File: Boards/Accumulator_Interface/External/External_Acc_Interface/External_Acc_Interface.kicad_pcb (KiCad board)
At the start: 2 copper layers, 107.2 x 62.8 mm, 5 parts, among them J1 Ampseal_35_VT, J2 SS-126-G-2, J3 BBS-126-G-A, U1 RJ45_VT, U2 RJ45_VT

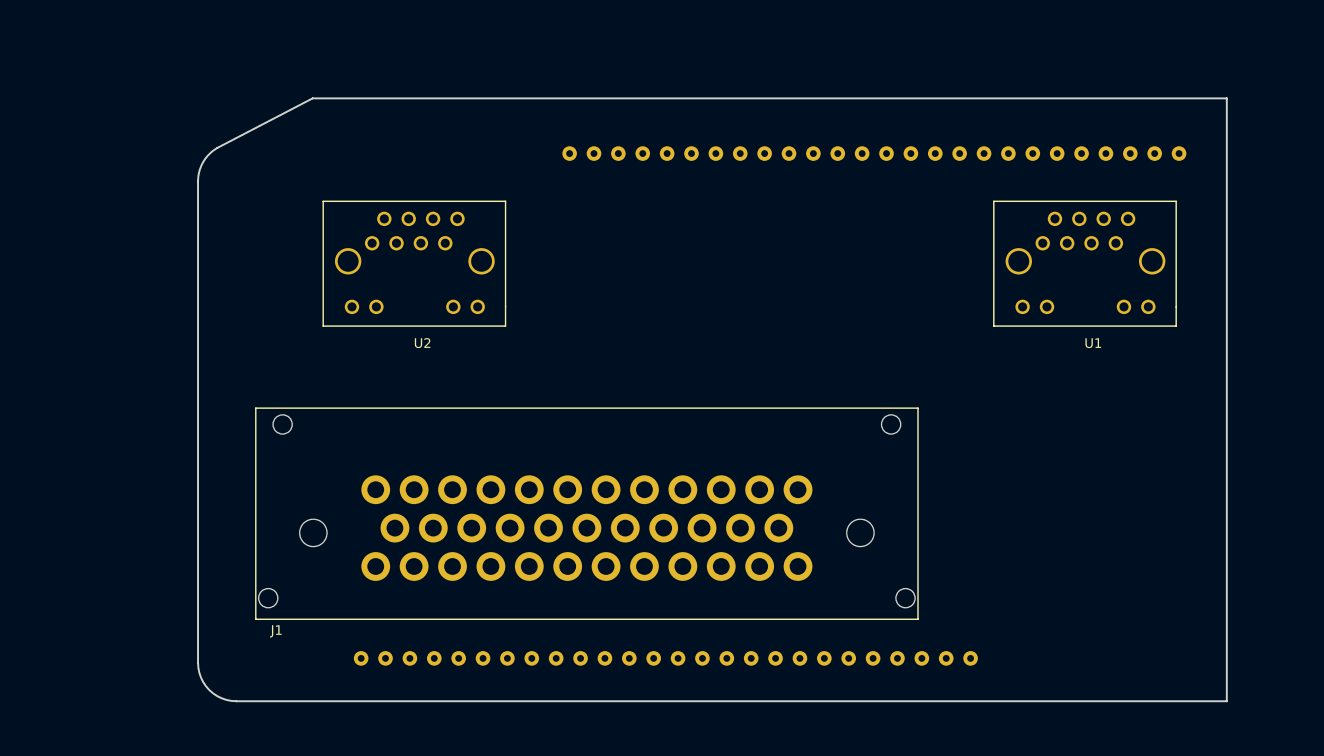
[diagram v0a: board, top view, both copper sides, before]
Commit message: started internal acc interface
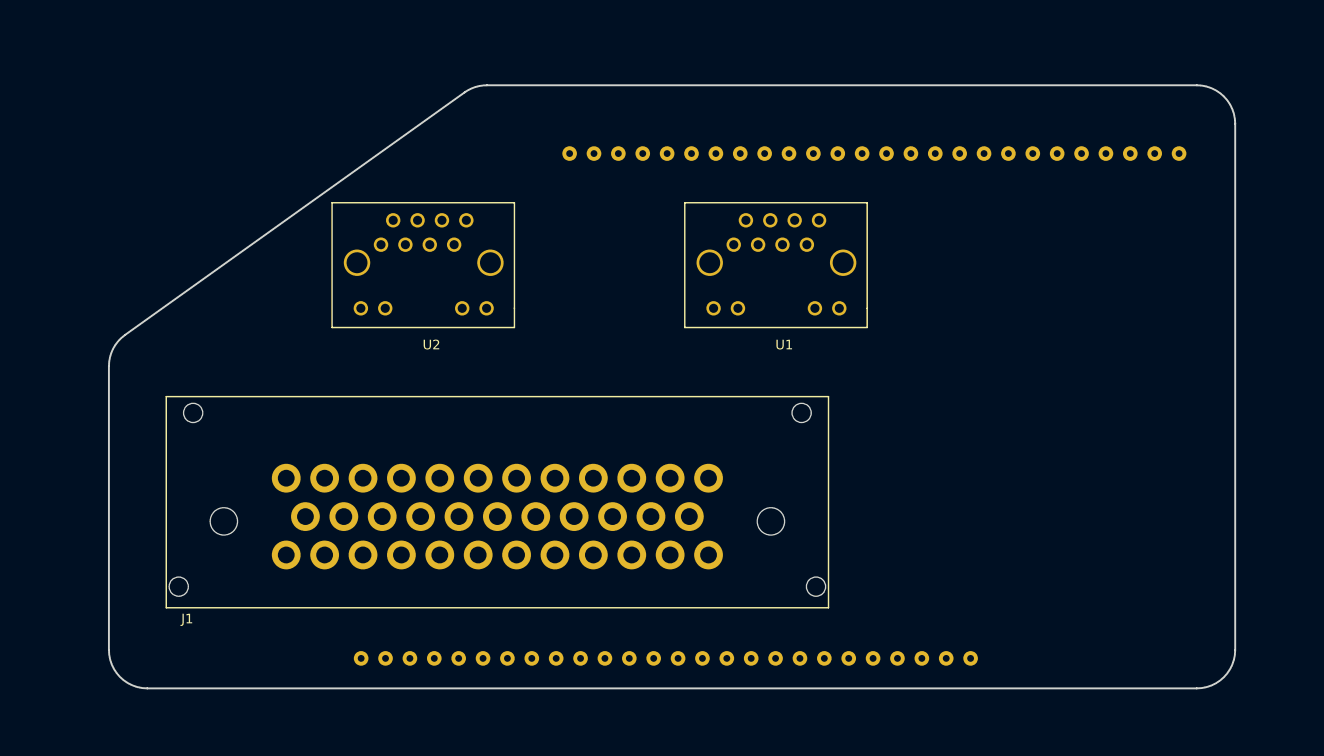
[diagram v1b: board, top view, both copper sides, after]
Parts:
- moved U1 32.2 mm to (53.5, 66.2)
- moved J1 9.40 mm to (2.50, 88.4)
- moved U2 0.94 mm to (16.8, 66.2)
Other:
- board size 107.2 x 62.8 mm -> 117.4 x 62.8 mm

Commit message: first pass of acc interface and rev1.1 of periph layout
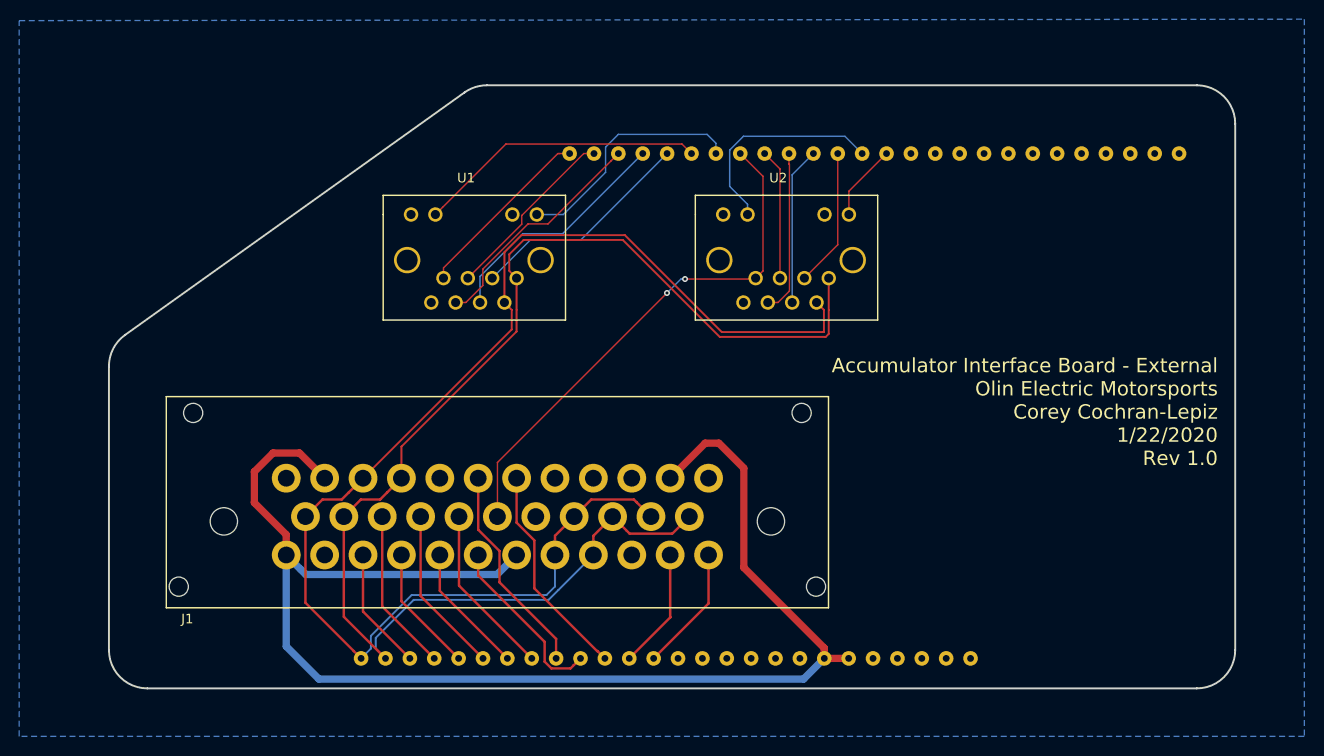
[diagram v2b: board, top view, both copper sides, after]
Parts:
- moved J2 56.9 mm to (16.8, 102.7)
- moved J3 56.9 mm to (38.5, 50.0)
- moved U2 51.8 mm to (67.6, 56.4), turned to 180 degrees
- moved U1 20.9 mm to (35.1, 56.4), turned to 180 degrees
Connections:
- J1 pad 1: /GND -> /CAN-GND
- J1 pad 10: /GND -> /CAN-GND
- J1 pad 12: /GND -> /CAN-GND
- J1 pad 13: /CAN-H -> /CAN_P
- J1 pad 14: /CAN-L -> /CAN_N
- J1 pad 18: /5V-AIR -> /5V_AIRC
- J1 pad 19: /GND -> /CAN-GND
- J1 pad 20: /CAN-H -> /CAN_P
- J1 pad 21: /CAN-L -> /CAN_N
- J1 pad 22: /CAN-H -> /CAN_P
- J1 pad 23: /CAN-L -> /CAN_N
- J1 pad 25: /GND -> /CAN-GND
- J1 pad 3: /CAN-H -> /CAN_P
- J1 pad 31: /CAN-H -> /CAN_P
- J1 pad 32: /CAN-L -> /CAN_N
- J1 pad 4: /CAN-L -> /CAN_N
- J1 pad 8: /GND -> /CAN-GND
- J1 pad 9: /GND -> /CAN-GND
- J2 pad 1: /GND -> /CAN_P
- J2 pad 10: /TSAL-Green-Neg -> /ChargeEnable2
- J2 pad 11: /TSAL-Red-Pos -> /TSMS->FinalShutdown
- J2 pad 12: /TSAL-Red-Neg -> /BSDP-Current-Sense
- J2 pad 13: /GND -> /HVD->HVD-Connector
- J2 pad 14: /HVD->HVD-Connector -> /CAN-GND
- J2 pad 15: /IMD->TSMS -> /CAN-GND
- J2 pad 16: /TSMS->FinalShutdown -> /CAN-GND
- J2 pad 17: /GND -> /CAN-GND
- J2 pad 18: /GND -> /CAN-GND
- J2 pad 19: /GND -> /CAN-GND
- J2 pad 2: /12V -> /CAN_N
- J2 pad 20: /GND -> /12V
- J2 pad 21: Net-(J2-Pad21) -> /12V
- J2 pad 3: /CAN-H -> /TSAL-Red-Pos
- J2 pad 4: /CAN-L -> /TSAL-Green-Pos
- J2 pad 5: /BSDP-Current-Sense -> /TSAL-Red-Neg
- J2 pad 6: /FAN-PWM -> /TSAL-Green-Neg
- J2 pad 8: /ChargeEnable2 -> /FAN-PWM
- J2 pad 9: /TSAL-Green-Pos -> /IMD->TSMS
- J3 pad 15: /GND -> /CAN-GND
- J3 pad 16: /GND -> /CAN-GND
- J3 pad 17: /GND -> /CAN-GND
- J3 pad 18: /GND -> /CAN-GND
- J3 pad 19: /GND -> /CAN-GND
- J3 pad 20: /GND -> /CAN-GND
- U1 pad 1: /CAN-L -> /CAN_N
- U1 pad 11: /GND -> /CAN-GND
- U1 pad 13: /GND -> /CAN-GND
- U1 pad 14: /GND -> /CAN-GND
- U1 pad 2: /CAN-H -> /CAN_P
- U1 pad 8: /GND -> /CAN-GND
- U1 pad 9: /GND -> /CAN-GND
- U2 pad 1: /CAN-L -> /CAN_N
- U2 pad 11: /GND -> /CAN-GND
- U2 pad 13: /GND -> /CAN-GND
- U2 pad 14: /GND -> /CAN-GND
- U2 pad 2: /CAN-H -> /CAN_P
- U2 pad 8: /GND -> /CAN-GND
- U2 pad 9: /GND -> /CAN-GND
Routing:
- net /12V: track 0.00 -> 148.9 mm
- net /CAN_N: track 0.00 -> 140.0 mm
- net /CAN_P: track 0.00 -> 138.4 mm
- net /5V_AIRC: track 0.00 -> 54.8 mm, vias 0 -> 2
- net /LED_O_BMS: track 0.00 -> 30.1 mm
- net /LED_G_BMS: track 0.00 -> 25.1 mm
- net /SCK_BMS: track 0.00 -> 25.0 mm
- net /MOSI_BMS: track 0.00 -> 24.4 mm
- net /RESET_BMS: track 0.00 -> 23.6 mm
- net /LED_O_AIRC: track 0.00 -> 22.6 mm
- net /TSMS->FinalShutdown: track 0.00 -> 22.6 mm
- net /IMD->TSMS: track 0.00 -> 22.1 mm
- net /5V_BMS: track 0.00 -> 19.1 mm
- net /MISO_BMS: track 0.00 -> 19.1 mm
- net /ChargeEnable2: track 0.00 -> 18.4 mm
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- added copper zone on B.Cu, net /CAN-GND
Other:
- net class Default: clearance 0.2 -> 0.1524; trace_width 0.25 -> 0.1524; via_dia 0.8 -> 0.6096; via_drill 0.4 -> 0.3048
- rule trace_clearance: 0.2 -> 0.1524
- rule trace_min: 0.2 -> 0.1524
- rule via_min_drill: 0.3 -> 0.3048
- rule via_min_size: 0.4 -> 0.6096
- board text added: "1 13 24"
- board text added: "12 23 36"
- board text added: "Accumulator Interface Board - External Olin Electric Motorsports Corey Cochran-Lepiz 1/22/2020 Rev 1.0"

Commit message: final rev interface v1
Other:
- board text added: "Accumulator Interface Board - External Corey Cochran-Lepiz OEM - MKV 1.22.2020 Rev 1.0"
- board text removed: "Accumulator Interface Board - External Olin Electric Motorsports Corey Cochran-Lepiz 1/22/2020 Rev 1.0"
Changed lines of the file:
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@@
     (effects (font (size 1.27 1.5) (thickness 0.3)) (justify mirror))
   )
-  (gr_text "Accumulator Interface Board - External\nOlin Electric Motorsports\nCorey Cochran-Lepiz\n1/22/2020\nRev 1.0" (at 106.075 76.975) (layer F.SilkS)
+  (gr_text "Accumulator Interface Board - External\nCorey Cochran-Lepiz\nOEM - MKV\n1.22.2020\nRev 1.0" (at 106.075 76.975) (layer F.SilkS)
     (effects (font (size 1.5 1.5) (thickness 0.3)) (justify right))
   )
